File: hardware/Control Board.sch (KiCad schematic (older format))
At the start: 44 parts, among them J1 Conn_FTDI, J2 SOLAR, M1 MOTOR, Q1 IRF7105PbF, Q2 BC817W, Q3 BC817W, Q4 IRF7105PbF, SW1 PROG, SW2 RESET, SW3 SW_Push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

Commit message: Routing MOSFETs
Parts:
- added Q1, Q6: BC817W, Package_TO_SOT_SMD:SOT-323_SC-70, symbol Transistor_BJT:BC817W
- added R11, R18: 10k, Resistor_SMD:R_0805_2012Metric, symbol Device:R
- C1: renamed from C3; footprint Capacitor_SMD:C_0402_1005Metric -> Capacitor_SMD:C_0805_2012Metric
- C2: renamed from C1; footprint Capacitor_SMD:C_0402_1005Metric -> Capacitor_SMD:C_0805_2012Metric
- C3: renamed from C8; footprint Capacitor_SMD:C_0402_1005Metric -> Capacitor_SMD:C_0805_2012Metric
- C4: renamed from C2; footprint Capacitor_SMD:C_0402_1005Metric -> Capacitor_SMD:C_0805_2012Metric
- C5: footprint Capacitor_SMD:C_0402_1005Metric -> Capacitor_SMD:C_0805_2012Metric
- C6: renamed from C4; footprint Capacitor_SMD:C_0402_1005Metric -> Capacitor_SMD:C_0805_2012Metric
- C7: renamed from C6; footprint Capacitor_SMD:C_0402_1005Metric -> Capacitor_SMD:C_0805_2012Metric
- C8: renamed from C7; footprint Capacitor_SMD:C_0402_1005Metric -> Capacitor_SMD:C_0805_2012Metric
- R1: footprint Resistor_SMD:R_0402_1005Metric -> Resistor_SMD:R_0805_2012Metric
- R10: renamed from R2; footprint Resistor_SMD:R_0402_1005Metric -> Resistor_SMD:R_0805_2012Metric
- R12: renamed from R3; footprint Resistor_SMD:R_0402_1005Metric -> Resistor_SMD:R_0805_2012Metric
- R13: renamed from R18; footprint Resistor_SMD:R_0402_1005Metric -> Resistor_SMD:R_0805_2012Metric
- R14: renamed from R17; footprint Resistor_SMD:R_0402_1005Metric -> Resistor_SMD:R_0805_2012Metric
- R15: renamed from R7; footprint Resistor_SMD:R_0402_1005Metric -> Resistor_SMD:R_0805_2012Metric
- R16: renamed from R8; footprint Resistor_SMD:R_0402_1005Metric -> Resistor_SMD:R_0805_2012Metric
- R17: renamed from R6; footprint Resistor_SMD:R_0402_1005Metric -> Resistor_SMD:R_0805_2012Metric
- R19: renamed from R9; footprint Resistor_SMD:R_0402_1005Metric -> Resistor_SMD:R_0805_2012Metric
- R2: renamed from R16; footprint Resistor_SMD:R_0402_1005Metric -> Resistor_SMD:R_0805_2012Metric
- R3: renamed from R19; footprint Resistor_SMD:R_0402_1005Metric -> Resistor_SMD:R_0805_2012Metric
- R4: renamed from R10; footprint Resistor_SMD:R_0402_1005Metric -> Resistor_SMD:R_0805_2012Metric
- R5: renamed from R11; footprint Resistor_SMD:R_0402_1005Metric -> Resistor_SMD:R_0805_2012Metric
- R6: renamed from R12; footprint Resistor_SMD:R_0402_1005Metric -> Resistor_SMD:R_0805_2012Metric
- R7: renamed from R4; footprint Resistor_SMD:R_0402_1005Metric -> Resistor_SMD:R_0805_2012Metric
- R8: renamed from R5; footprint Resistor_SMD:R_0402_1005Metric -> Resistor_SMD:R_0805_2012Metric
- R9: renamed from R13; footprint Resistor_SMD:R_0402_1005Metric -> Resistor_SMD:R_0805_2012Metric
- renumbered J2 to J1, J1 to J2, Q1 to Q2, Q2 to Q3, Q3 to Q4, Q4 to Q5
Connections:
- net +BATT: now also Q2.3 (S2), R12.1, R17.1; no longer Q5.1 (S1), Q5.3 (S2)
- net GND: now also Q2.1 (S1), Q5.1 (S1), Q1.2 (E), Q6.2 (E), R11.2, R18.2; no longer Q2.5 (D2), Q2.6 (D2), Q2.7 (D1), Q2.8 (D1), R10.2, R19.2
- net WATER_OFF: now also Q2.2 (G1), U3.15 (IO12), R11.1; no longer R17.1, U3.16 (IO13)
- net WATER_ON: now also Q5.2 (G1), R10.2, U3.16 (IO13), R18.1; no longer R10.1, R12.2, U3.15 (IO12)
- net M+: no longer names the net of Q5.5 (D2), Q5.6 (D2)
- net M+: now also M1.2 (-), Q5.7 (D1), Q5.8 (D1); no longer M1.1 (+), Q2.1 (S1)
- removed net M-: M1.2 (-), Q2.3 (S2), Q5.7 (D1), Q5.8 (D1)
- new net: Q5.4 (G2), Q6.3 (C), R17.2
- new net: Q1.3 (C), Q2.4 (G2), R12.2
- new net: M1.1 (+), Q2.5 (D2), Q2.6 (D2), Q2.7 (D1), Q2.8 (D1)
- new net: Q1.1 (B), R10.1
- new net: Q6.1 (B), R19.2
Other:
- moved on the sheet: M1, Q2, Q5, R10, R12, R17, R19

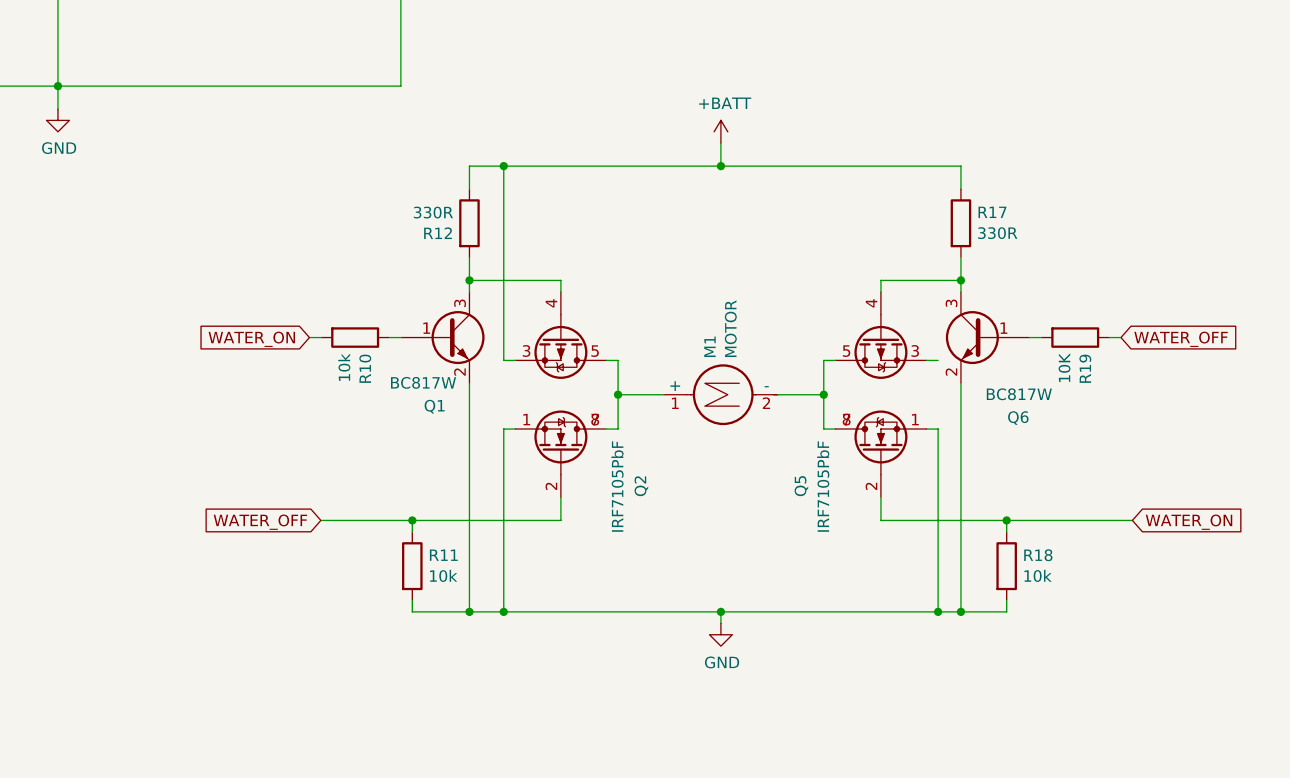
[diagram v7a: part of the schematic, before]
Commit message: Adding mounting holes
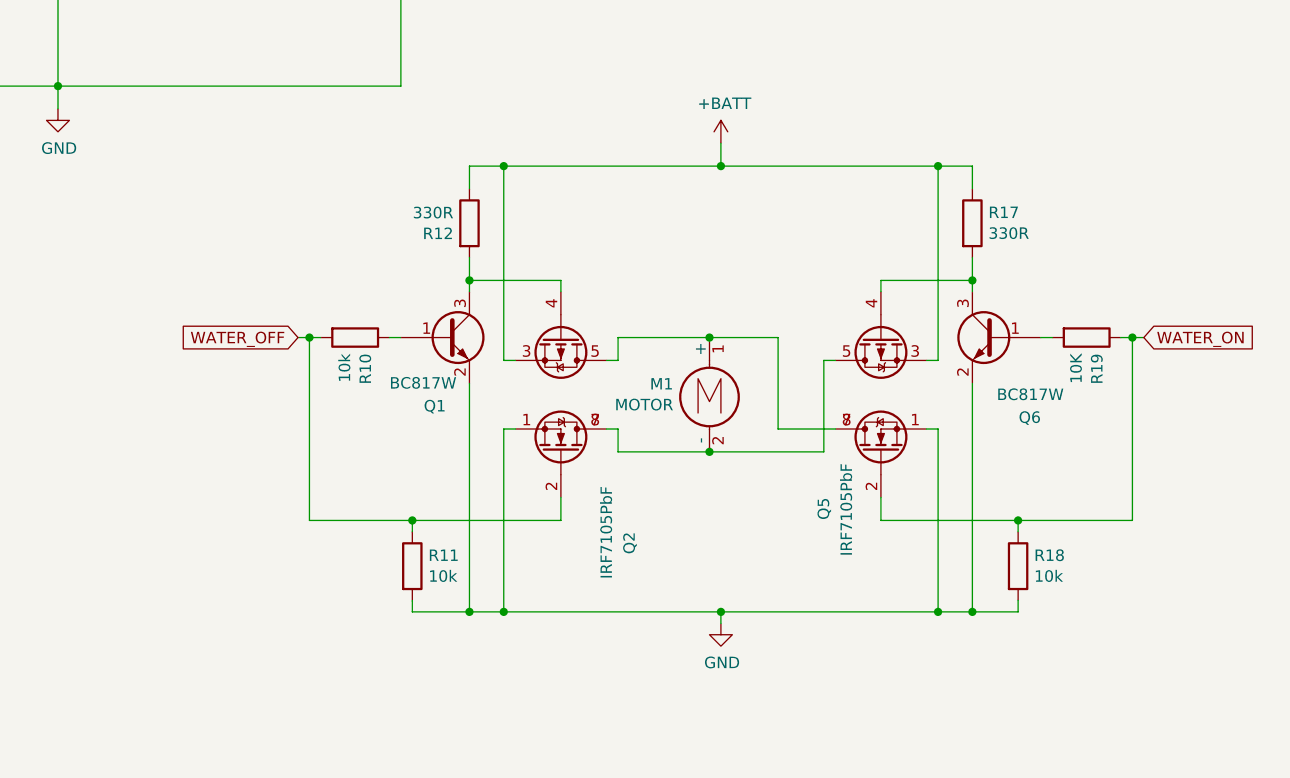
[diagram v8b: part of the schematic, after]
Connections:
- net +BATT: now also Q5.3 (S2)
- net WATER_OFF: now also R10.2; no longer R19.1
- net WATER_ON: now also R19.1; no longer R10.2
- net at M1.2 (-), Q5.5 (D2), Q5.6 (D2): now also Q2.7 (D1), Q2.8 (D1); no longer Q5.7 (D1), Q5.8 (D1)
- net at M1.1 (+), Q2.5 (D2), Q2.6 (D2): now also Q5.7 (D1), Q5.8 (D1); no longer Q2.7 (D1), Q2.8 (D1)
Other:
- moved on the sheet: M1, Q6, R17, R18, R19
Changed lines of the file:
@@
 L Device:R R17
 U 1 1 602E4117
-P 9900 4650
-F 0 "R17" H 9970 4696 50  0000 L CNN
-F 1 "330R" H 9970 4605 50  0000 L CNN
-F 2 "Resistor_SMD:R_0805_2012Metric" V 9830 4650 50  0001 C CNN
-F 3 "~" H 9900 4650 50  0001 C CNN
-	1    9900 4650
+P 9950 4650
+F 0 "R17" H 10020 4696 50  0000 L CNN
+F 1 "330R" H 10020 4605 50  0000 L CNN
+F 2 "Resistor_SMD:R_0805_2012Metric" V 9880 4650 50  0001 C CNN
+F 3 "~" H 9950 4650 50  0001 C CNN
+	1    9950 4650
 	1    0    0    -1
 $EndComp
@@
 L Device:R R19
 U 1 1 602F2B38
-P 10400 5150
-F 0 "R19" H 10470 5196 50  0000 L CNN
-F 1 "10K" H 10470 5105 50  0000 L CNN
-F 2 "Resistor_SMD:R_0805_2012Metric" V 10330 5150 50  0001 C CNN
-F 3 "~" H 10400 5150 50  0001 C CNN
-	1    10400 5150
+P 10450 5150
+F 0 "R19" H 10520 5196 50  0000 L CNN
+F 1 "10K" H 10520 5105 50  0000 L CNN
+F 2 "Resistor_SMD:R_0805_2012Metric" V 10380 5150 50  0001 C CNN
+F 3 "~" H 10450 5150 50  0001 C CNN
+	1    10450 5150
 	0    1    1    0
 $EndComp
@@
 L Motor:Motor_DC M1
 U 1 1 60395F40
-P 8800 5400
-F 0 "M1" H 8958 5396 50  0000 L CNN
-F 1 "MOTOR" H 8958 5305 50  0000 L CNN
-F 2 "Connector_JST:JST_EH_B02B-EH-A_1x02_P2.50mm_Vertical" H 8800 5310 50  0001 C CNN
-F 3 "~" H 8800 5310 50  0001 C CNN
-	1    8800 5400
-	0    -1   -1   0
+P 8800 5350
+F 0 "M1" H 8642 5346 50  0000 R CNN
+F 1 "MOTOR" H 8642 5255 50  0000 R CNN
+F 2 "Connector_JST:JST_EH_B02B-EH-A_1x02_P2.50mm_Vertical" H 8800 5260 50  0001 C CNN
+F 3 "~" H 8800 5260 50  0001 C CNN
+	1    8800 5350
+	1    0    0    -1
 $EndComp
 Wire Wire Line
@@
 	4650 1500 5050 1500
 Connection ~ 4950 4050
-Text GLabel 7050 5150 0    50   Input ~ 0
-WATER_ON
-Text GLabel 10600 5150 2    50   Input ~ 0
+Text GLabel 7000 5150 0    50   Input ~ 0
 WATER_OFF
 $Comp
@@
 U 1 1 602B637F
 P 9550 5650
-F 0 "Q5" H 9450 6000 50  0000 R CNN
-F 1 "IRF7105PbF" H 9600 5900 50  0000 R CNN
+F 0 "Q5" H 9350 5900 50  0000 R CNN
+F 1 "IRF7105PbF" H 9500 5800 50  0000 R CNN
 F 2 "Package_SO:SOIC-8_3.9x4.9mm_P1.27mm" H 9300 5000 50  0001 L CNN
 F 3 "http://www.irf.com/product-info/datasheets/data/irf8721pbf-1.pdf" H 9450 5650 50  0001 L CNN
@@
 $EndComp
 Wire Wire Line
-	8350 5250 8400 5250
-Wire Wire Line
-	8400 5550 8350 5550
-Wire Wire Line
-	9350 5550 9300 5550
-Wire Wire Line
-	9300 5250 9350 5250
-Wire Wire Line
 	7950 5250 7900 5250
 Wire Wire Line
@@
 Wire Wire Line
 	9750 5550 9800 5550
-Wire Wire Line
-	8400 5250 8400 5400
-Wire Wire Line
-	9300 5250 9300 5400
-Wire Wire Line
-	9100 5400 9300 5400
-Connection ~ 9300 5400
-Wire Wire Line
-	9300 5400 9300 5550
-Wire Wire Line
-	8400 5400 8600 5400
-Connection ~ 8400 5400
-Wire Wire Line
-	8400 5400 8400 5550
 Wire Wire Line
 	7900 4400 8850 4400
@@
 Wire Wire Line
 	8150 5850 8150 5950
-Text GLabel 7100 5950 0    50   Input ~ 0
-WATER_OFF
 $Comp
 L irf7105pbf:IRF7105PbF Q2
 U 1 1 602BC5F8
 P 8150 5650
-F 0 "Q2" H 8050 6000 50  0000 R CNN
-F 1 "IRF7105PbF" H 8200 5900 50  0000 R CNN
+F 0 "Q2" H 7800 5950 50  0000 R CNN
+F 1 "IRF7105PbF" H 8000 5850 50  0000 R CNN
 F 2 "Package_SO:SOIC-8_3.9x4.9mm_P1.27mm" H 7900 5000 50  0001 L CNN
 F 3 "http://www.irf.com/product-info/datasheets/data/irf8721pbf-1.pdf" H 8050 5650 50  0001 L CNN
@@
 	0    1    -1   0
 $EndComp
-Wire Wire Line
-	7100 5950 7500 5950
-Text GLabel 10650 5950 2    50   Input ~ 0
-WATER_ON
-Wire Wire Line
-	10650 5950 10100 5950
 Wire Wire Line
 	9550 5950 9550 5850
@@
 L Transistor_BJT:BC817W Q6
 U 1 1 61242BA9
-P 10000 5150
-F 0 "Q6" H 9800 4800 50  0000 L CNN
-F 1 "BC817W" H 9700 4900 50  0000 L CNN
-F 2 "Package_TO_SOT_SMD:SOT-323_SC-70" H 10200 5075 50  0001 L CIN
-F 3 "http://www.fairchildsemi.com/ds/BC/BC817.pdf" H 10000 5150 50  0001 L CNN
-	1    10000 5150
+P 10050 5150
+F 0 "Q6" H 9850 4800 50  0000 L CNN
+F 1 "BC817W" H 9750 4900 50  0000 L CNN
+F 2 "Package_TO_SOT_SMD:SOT-323_SC-70" H 10250 5075 50  0001 L CIN
+F 3 "http://www.fairchildsemi.com/ds/BC/BC817.pdf" H 10050 5150 50  0001 L CNN
+	1    10050 5150
 	-1   0    0    -1
 $EndComp
@@
 	7750 4900 8150 4900
 Wire Wire Line
-	7050 5150 7100 5150
-Wire Wire Line
 	7400 5150 7450 5150
 Wire Wire Line
@@
 Connection ~ 7900 4400
 Wire Wire Line
-	10550 5150 10600 5150
-Wire Wire Line
-	10200 5150 10250 5150
-Wire Wire Line
-	9900 4950 9900 4900
+	10600 5150 10650 5150
+Wire Wire Line
+	10250 5150 10300 5150
+Wire Wire Line
+	9950 4950 9950 4900
 Wire Wire Line
 	9550 4950 9550 4900
-Wire Wire Line
-	9550 4900 9900 4900
-Connection ~ 9900 4900
-Wire Wire Line
-	9900 4900 9900 4800
-Wire Wire Line
-	9900 4400 9900 4500
-Wire Wire Line
-	8850 4400 9900 4400
+Connection ~ 9950 4900
+Wire Wire Line
+	9950 4900 9950 4800
+Wire Wire Line
+	9950 4400 9950 4500
+Wire Wire Line
+	8850 4400 9800 4400
 $Comp
 L Device:R R11
@@
 L Device:R R18
 U 1 1 615568A8
-P 10100 6150
-F 0 "R18" H 10170 6196 50  0000 L CNN
-F 1 "10k" H 10170 6105 50  0000 L CNN
-F 2 "Resistor_SMD:R_0805_2012Metric" V 10030 6150 50  0001 C CNN
-F 3 "~" H 10100 6150 50  0001 C CNN
-	1    10100 6150
+P 10150 6150
+F 0 "R18" H 10220 6196 50  0000 L CNN
+F 1 "10k" H 10220 6105 50  0000 L CNN
+F 2 "Resistor_SMD:R_0805_2012Metric" V 10080 6150 50  0001 C CNN
+F 3 "~" H 10150 6150 50  0001 C CNN
+	1    10150 6150
 	1    0    0    -1
 $EndComp
 Wire Wire Line
 	7500 6000 7500 5950
-Connection ~ 7500 5950
 Wire Wire Line
 	7500 5950 8150 5950
 Wire Wire Line
-	10100 6000 10100 5950
-Connection ~ 10100 5950
-Wire Wire Line
-	10100 5950 9550 5950
+	10150 6000 10150 5950
 Wire Wire Line
 	7500 6300 7500 6350
@@
 	8850 6350 9800 6350
 Wire Wire Line
-	10100 6350 10100 6300
+	10150 6350 10150 6300
 Wire Wire Line
 	7750 5350 7750 6350
@@
 Wire Wire Line
 	9800 5550 9800 6350
+Wire Wire Line
+	4550 2700 5050 2700
+Wire Wire Line
+	4200 2800 5050 2800
+Wire Wire Line
+	9950 5350 9950 6350
+Connection ~ 9950 6350
+Wire Wire Line
+	9950 6350 10150 6350
+Wire Wire Line
+	10150 5950 10650 5950
+Wire Wire Line
+	10650 5950 10650 5150
+Connection ~ 10150 5950
+Wire Wire Line
+	7500 5950 7050 5950
+Wire Wire Line
+	7050 5950 7050 5150
+Connection ~ 7500 5950
+Wire Wire Line
+	7050 5150 7100 5150
+Wire Wire Line
+	8350 5550 8400 5550
+Wire Wire Line
+	8400 5550 8400 5650
+Wire Wire Line
+	8400 5650 8800 5650
+Wire Wire Line
+	9300 5650 9300 5250
+Wire Wire Line
+	9300 5250 9350 5250
+Wire Wire Line
+	9350 5550 9100 5550
+Wire Wire Line
+	8350 5250 8400 5250
+Wire Wire Line
+	8400 5250 8400 5150
+Wire Wire Line
+	8400 5150 8800 5150
+Wire Wire Line
+	9100 5150 9100 5550
+Connection ~ 8800 5150
+Wire Wire Line
+	8800 5150 9100 5150
+Connection ~ 8800 5650
+Wire Wire Line
+	8800 5650 9300 5650
+Wire Wire Line
+	9800 5250 9800 4400
+Wire Wire Line
+	9550 5950 10150 5950
+Wire Wire Line
+	9550 4900 9950 4900
+Wire Wire Line
+	9800 4400 9950 4400
+Connection ~ 9800 4400
+Wire Wire Line
+	9800 6350 9950 6350
 Connection ~ 9800 6350
-Wire Wire Line
-	4550 2700 5050 2700
-Wire Wire Line
-	4200 2800 5050 2800
-Wire Wire Line
-	9800 6350 9900 6350
-Wire Wire Line
-	9900 5350 9900 6350
-Connection ~ 9900 6350
-Wire Wire Line
-	9900 6350 10100 6350
+Text GLabel 10700 5150 2    50   Input ~ 0
+WATER_ON
+Wire Wire Line
+	10650 5150 10700 5150
+Connection ~ 10650 5150
+Wire Wire Line
+	7000 5150 7050 5150
+Connection ~ 7050 5150
 $EndSCHEMATC
